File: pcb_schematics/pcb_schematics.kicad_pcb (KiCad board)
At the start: 2 copper layers, 140 x 108 mm, 56 parts, among them J1 CUE_SJ1-352XNG, J2 Conn_01x01_Pin, SW1 SW_Push, SW2 SW_Push, SW3 SW_Push, SW4 SW_Push, SW5 RotaryEncoder, SW6 RotaryEncoder, U1 RPi_Pico_TH, U2 RDA5807M_Module, U3 LM386, U4 LM386

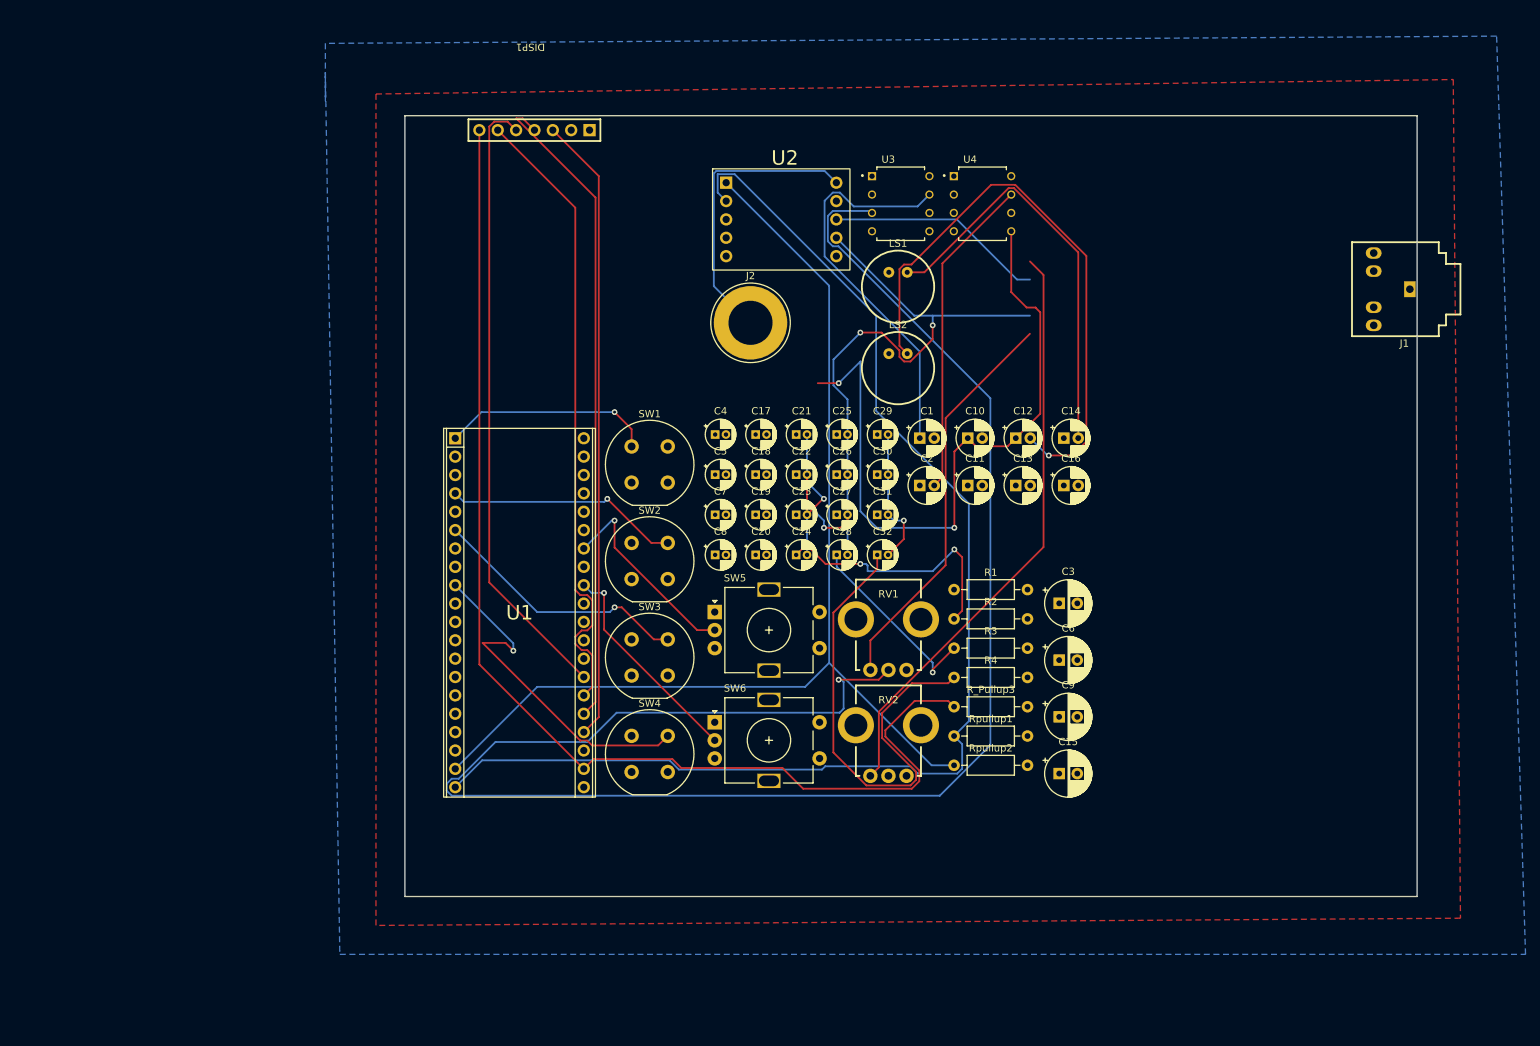
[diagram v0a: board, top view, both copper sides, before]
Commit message: Converted to connectors
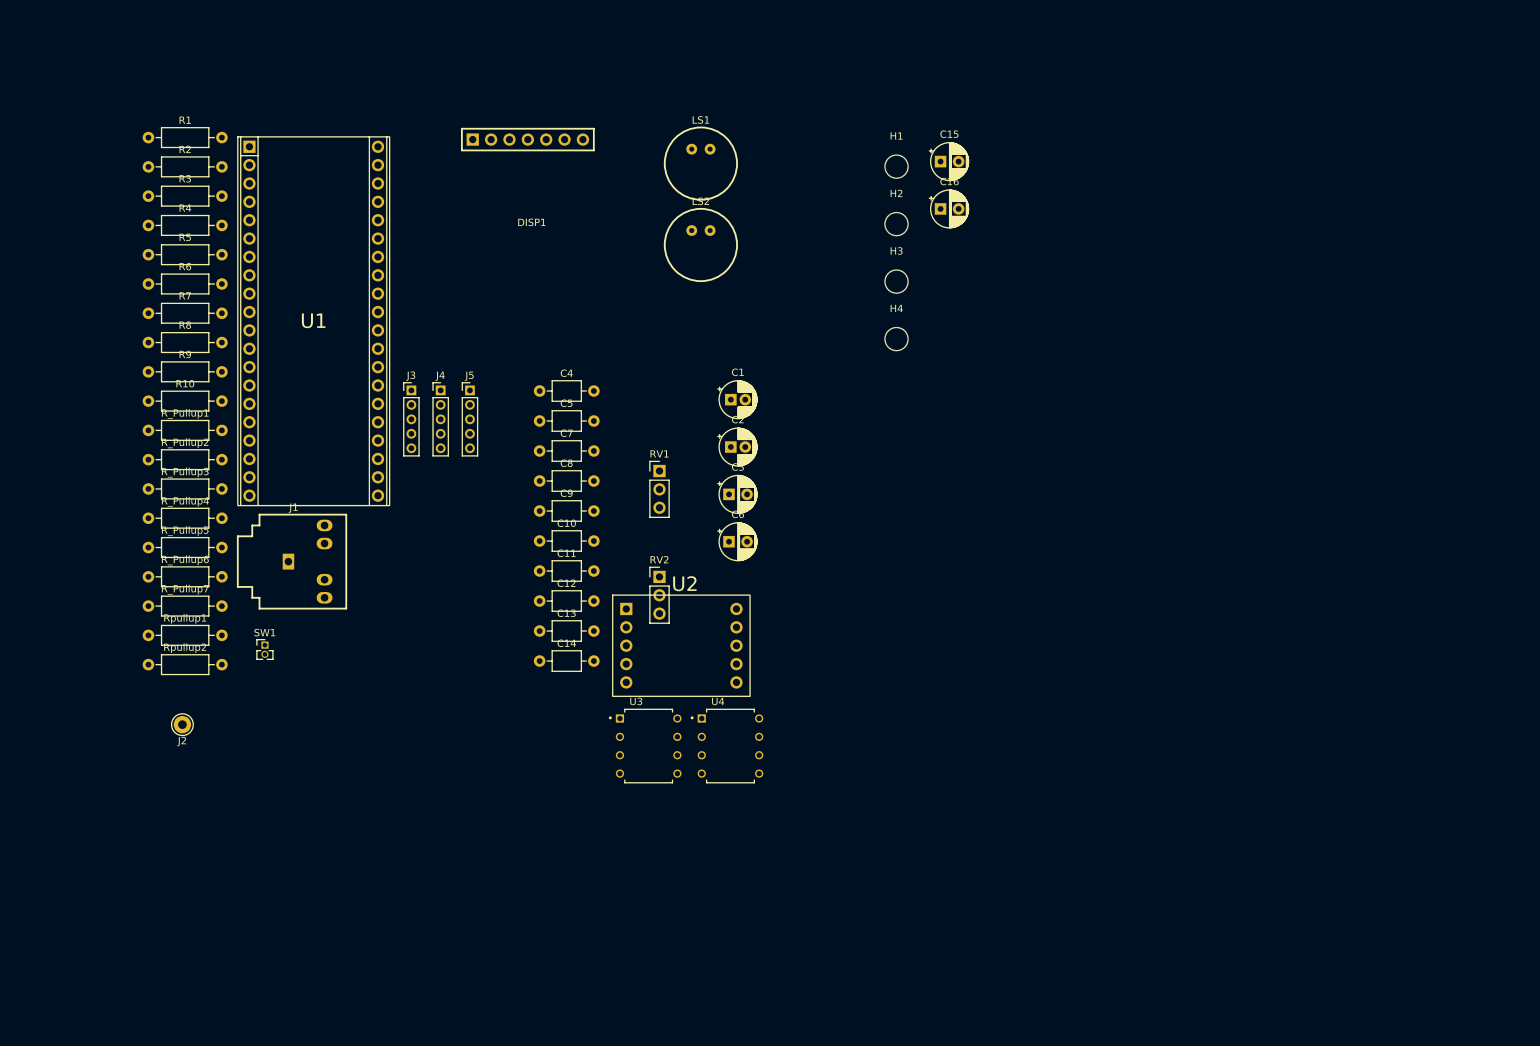
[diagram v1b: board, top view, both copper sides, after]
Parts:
- removed C17, C18, C19, C20, C21, C22, C23, C24, C25, C26, C27, C28, C29, C30, C31, C32: 10 nF, Capacitor_THT:CP_Radial_D4.0mm_P1.50mm
- removed SW2, SW3, SW4: SW_Push, Button_Switch_THT:Push_E-Switch_KS01Q01
- removed SW5, SW6: RotaryEncoder, Rotary_Encoder:RotaryEncoder_Alps_EC11E-Switch_Vertical_H20mm
- added H1: MountingHole, MountingHole:MountingHole_3.2mm_M3, F.Cu at (145.0, 36.0)
- added H2: MountingHole, MountingHole:MountingHole_3.2mm_M3, F.Cu at (145.0, 44.0)
- added H3: MountingHole, MountingHole:MountingHole_3.2mm_M3, F.Cu at (145.0, 52.0)
- added H4: MountingHole, MountingHole:MountingHole_3.2mm_M3, F.Cu at (145.0, 59.9)
- added J3: Conn_01x05, Connector_PinHeader_2.00mm:PinHeader_1x05_P2.00mm_Vertical, F.Cu at (77.9, 67.0)
- added J4: Conn_01x05, Connector_PinHeader_2.00mm:PinHeader_1x05_P2.00mm_Vertical, F.Cu at (82.0, 67.0)
- added J5: Conn_01x05, Connector_PinHeader_2.00mm:PinHeader_1x05_P2.00mm_Vertical, F.Cu at (86.0, 67.0)
- added R10: 10Ω, Resistor_THT:R_Axial_DIN0207_L6.3mm_D2.5mm_P10.16mm_Horizontal, F.Cu at (41.5, 68.5)
- added R5: 10Ω, Resistor_THT:R_Axial_DIN0207_L6.3mm_D2.5mm_P10.16mm_Horizontal, F.Cu at (41.5, 48.2)
- added R6: 10Ω, Resistor_THT:R_Axial_DIN0207_L6.3mm_D2.5mm_P10.16mm_Horizontal, F.Cu at (41.5, 52.3)
- added R7: 10Ω, Resistor_THT:R_Axial_DIN0207_L6.3mm_D2.5mm_P10.16mm_Horizontal, F.Cu at (41.5, 56.3)
- added R8: 10Ω, Resistor_THT:R_Axial_DIN0207_L6.3mm_D2.5mm_P10.16mm_Horizontal, F.Cu at (41.5, 60.4)
- added R9: 10Ω, Resistor_THT:R_Axial_DIN0207_L6.3mm_D2.5mm_P10.16mm_Horizontal, F.Cu at (41.5, 64.4)
- added R_Pullup1: 2kΩ, Resistor_THT:R_Axial_DIN0207_L6.3mm_D2.5mm_P10.16mm_Horizontal, F.Cu at (41.5, 72.5)
- added R_Pullup2: 2kΩ, Resistor_THT:R_Axial_DIN0207_L6.3mm_D2.5mm_P10.16mm_Horizontal, F.Cu at (41.5, 76.6)
- added R_Pullup4: 2kΩ, Resistor_THT:R_Axial_DIN0207_L6.3mm_D2.5mm_P10.16mm_Horizontal, F.Cu at (41.5, 84.7)
- added R_Pullup5: 2kΩ, Resistor_THT:R_Axial_DIN0207_L6.3mm_D2.5mm_P10.16mm_Horizontal, F.Cu at (41.5, 88.7)
- added R_Pullup6: 2kΩ, Resistor_THT:R_Axial_DIN0207_L6.3mm_D2.5mm_P10.16mm_Horizontal, F.Cu at (41.5, 92.8)
- added R_Pullup7: 2kΩ, Resistor_THT:R_Axial_DIN0207_L6.3mm_D2.5mm_P10.16mm_Horizontal, F.Cu at (41.5, 96.8)
- C10, C11, C12, C13, C14: value 10 µF -> 0.05 µF; footprint Capacitor_THT:CP_Radial_D5.0mm_P2.00mm -> Capacitor_THT:C_Axial_L3.8mm_D2.6mm_P7.50mm_Horizontal
- C15, C3, C6: footprint Capacitor_THT:CP_Radial_D6.3mm_P2.50mm -> Capacitor_THT:CP_Radial_D5.0mm_P2.50mm
- C16: value 10 µF -> 470 µF; footprint Capacitor_THT:CP_Radial_D5.0mm_P2.00mm -> Capacitor_THT:CP_Radial_D5.0mm_P2.50mm
- C4, C5, C7, C8: value 10 nF -> 0.05 µF; footprint Capacitor_THT:CP_Radial_D4.0mm_P1.50mm -> Capacitor_THT:C_Axial_L3.8mm_D2.6mm_P7.50mm_Horizontal
- C9: value 470 µF -> 0.05 µF; footprint Capacitor_THT:CP_Radial_D6.3mm_P2.50mm -> Capacitor_THT:C_Axial_L3.8mm_D2.6mm_P7.50mm_Horizontal
- J2: footprint Connector:Banana_Jack_1Pin -> Connector_Pin:Pin_D1.0mm_L10.0mm_LooseFit
- RV1, RV2: footprint ECE:Bourns_PTV09_Horiz -> Connector_PinHeader_2.54mm:PinHeader_1x03_P2.54mm_Vertical
- SW1: footprint Button_Switch_THT:Push_E-Switch_KS01Q01 -> Connector_PinHeader_1.27mm:PinHeader_1x02_P1.27mm_Vertical
- moved J1 159.6 mm to (60.9, 90.7), turned to 0 degrees
- moved R1 127.8 mm to (41.5, 32.0)
- moved R2 127.8 mm to (41.5, 36.1)
- moved R3 127.8 mm to (41.5, 40.1)
- moved R4 127.8 mm to (41.5, 44.2)
- moved R_Pullup3 115.4 mm to (41.5, 80.6)
- moved Rpullup1 112.3 mm to (41.5, 100.9)
- moved Rpullup2 112.3 mm to (41.5, 104.9)
- moved J2 96.2 mm to (46.2, 113.2)
- moved C15 86.2 mm to (151.1, 35.4)
- moved U3 82.7 mm to (110.7, 116.2)
- moved U4 82.7 mm to (122.0, 116.2)
- moved C14 78.8 mm to (95.6, 104.4)
- moved C9 77.3 mm to (95.6, 83.7)
- moved DISP1 74.7 mm to (76.3, 64.3), turned to 0 degrees
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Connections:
- C10 pad 1: Net-(C10-Pad1) -> /ROT1A
- C11 pad 1: Net-(C10-Pad2) -> /ROT2A
- C12 pad 1: Net-(C10-Pad1) -> /ROT2B
- C12 pad 2: Net-(C11-Pad2) -> Net-(C12-Pad2)
- C13 pad 1: Net-(C13-Pad1) -> /ROT3A
- C14 pad 1: Net-(C13-Pad1) -> /ROT3B
- C15 pad 2: Net-(C14-Pad2) -> Net-(U3-+)
- C16 pad 1: Net-(C13-Pad2) -> Net-(C16-Pad1)
- C16 pad 2: Net-(C14-Pad2) -> Net-(U4-+)
- C2 pad 1: GND -> Net-(U4-BYPASS)
- C2 pad 2: Net-(U4-BYPASS) -> GND
- C3 pad 1: Net-(C10-Pad1) -> Net-(C3-Pad1)
- C4 pad 1: Net-(C17-Pad1) -> Net-(C3-Pad1)
- C4 pad 2: Net-(C10-Pad1) -> Net-(C4-Pad2)
- C5 pad 1: Net-(C21-Pad1) -> Net-(C5-Pad1)
- C5 pad 2: Net-(C13-Pad1) -> Net-(C5-Pad2)
- C6 pad 1: Net-(C13-Pad1) -> Net-(C5-Pad1)
- C6 pad 2: Net-(C15-Pad1) -> Net-(C6-Pad2)
- C7 pad 1: Net-(C25-Pad1) -> /LOUT
- C7 pad 2: /ROUT -> Net-(C7-Pad2)
- C8 pad 1: Net-(C29-Pad1) -> /ROUT
- C8 pad 2: /LOUT -> Net-(C8-Pad2)
- C9 pad 1: Net-(C3-Pad2) -> /ROT1B
- C9 pad 2: Net-(C11-Pad2) -> Net-(C9-Pad2)
- LS1 pad 1: Net-(C14-Pad2) -> Net-(C6-Pad2)
- LS2 pad 1: Net-(C11-Pad2) -> Net-(C3-Pad2)
- R1 pad 1: Net-(C17-Pad1) -> Net-(C4-Pad2)
- R2 pad 1: Net-(C21-Pad1) -> Net-(C5-Pad2)
- R3 pad 1: Net-(C25-Pad1) -> Net-(C8-Pad2)
- R4 pad 1: Net-(C29-Pad1) -> Net-(C7-Pad2)
- RV1 pad 2: Net-(U3-+) -> Net-(C15-Pad1)
- RV2 pad 2: Net-(U4-+) -> Net-(C16-Pad1)
- U1 pad 10: unconnected-(U1-GP7-Pad10) -> /ROT2B
- U1 pad 2: unconnected-(U1-GP1-Pad2) -> /SW2
- U1 pad 32: /RotB -> /ROT3B
- U1 pad 34: /RotA -> /ROT3A
- U1 pad 39: unconnected-(U1-VSYS-Pad39) -> 5V
- U1 pad 4: /SW2 -> /SW3
- U1 pad 5: unconnected-(U1-GP3-Pad5) -> /SW4
- U1 pad 6: /SW3 -> /ROT1A
- U1 pad 7: unconnected-(U1-GP5-Pad7) -> /ROT1B
- U1 pad 9: /SW4 -> /ROT2A
- U3 pad 5: Net-(C13-Pad1) -> Net-(C5-Pad1)
- U3 pad 6: /3V3 -> 5V
- U4 pad 5: Net-(C10-Pad1) -> Net-(C3-Pad1)
- U4 pad 6: /3V3 -> 5V
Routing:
- net Net-(U3-+): track 240.0 -> 0.00 mm, vias 1 -> 0
- net /I2CSCK: track 176.6 -> 0.00 mm
- net /CS: track 163.9 -> 0.00 mm
- net /I2CTX: track 153.2 -> 0.00 mm
- net Net-(C10-Pad1): track 94.9 -> 0.00 mm, vias 2 -> 0
- net /SDA: track 90.7 -> 0.00 mm
- net /ROUT: track 89.0 -> 0.00 mm, vias 3 -> 0
- net /DC: track 87.5 -> 0.00 mm
- net /SCK: track 86.8 -> 0.00 mm
- net /RES: track 86.0 -> 0.00 mm
- net Net-(C11-Pad2): track 82.1 -> 0.00 mm, vias 1 -> 0
- net /RSpeaker: track 81.8 -> 0.00 mm
- net Net-(C29-Pad1): track 66.7 -> 0.00 mm
- net Net-(C14-Pad2): track 57.9 -> 0.00 mm
- net /LSpeaker: track 55.7 -> 0.00 mm
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- removed copper zone on B.Cu, net /3V3
- removed copper zone on F.Cu, net GND
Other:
- board outline removed

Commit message: Updates PCb according to ROB's feedback
Added PCb layour according to the discussion with butoons and display on top and display below using front copper. Added Radio module using back copper. Speakers left to set up using back copper.
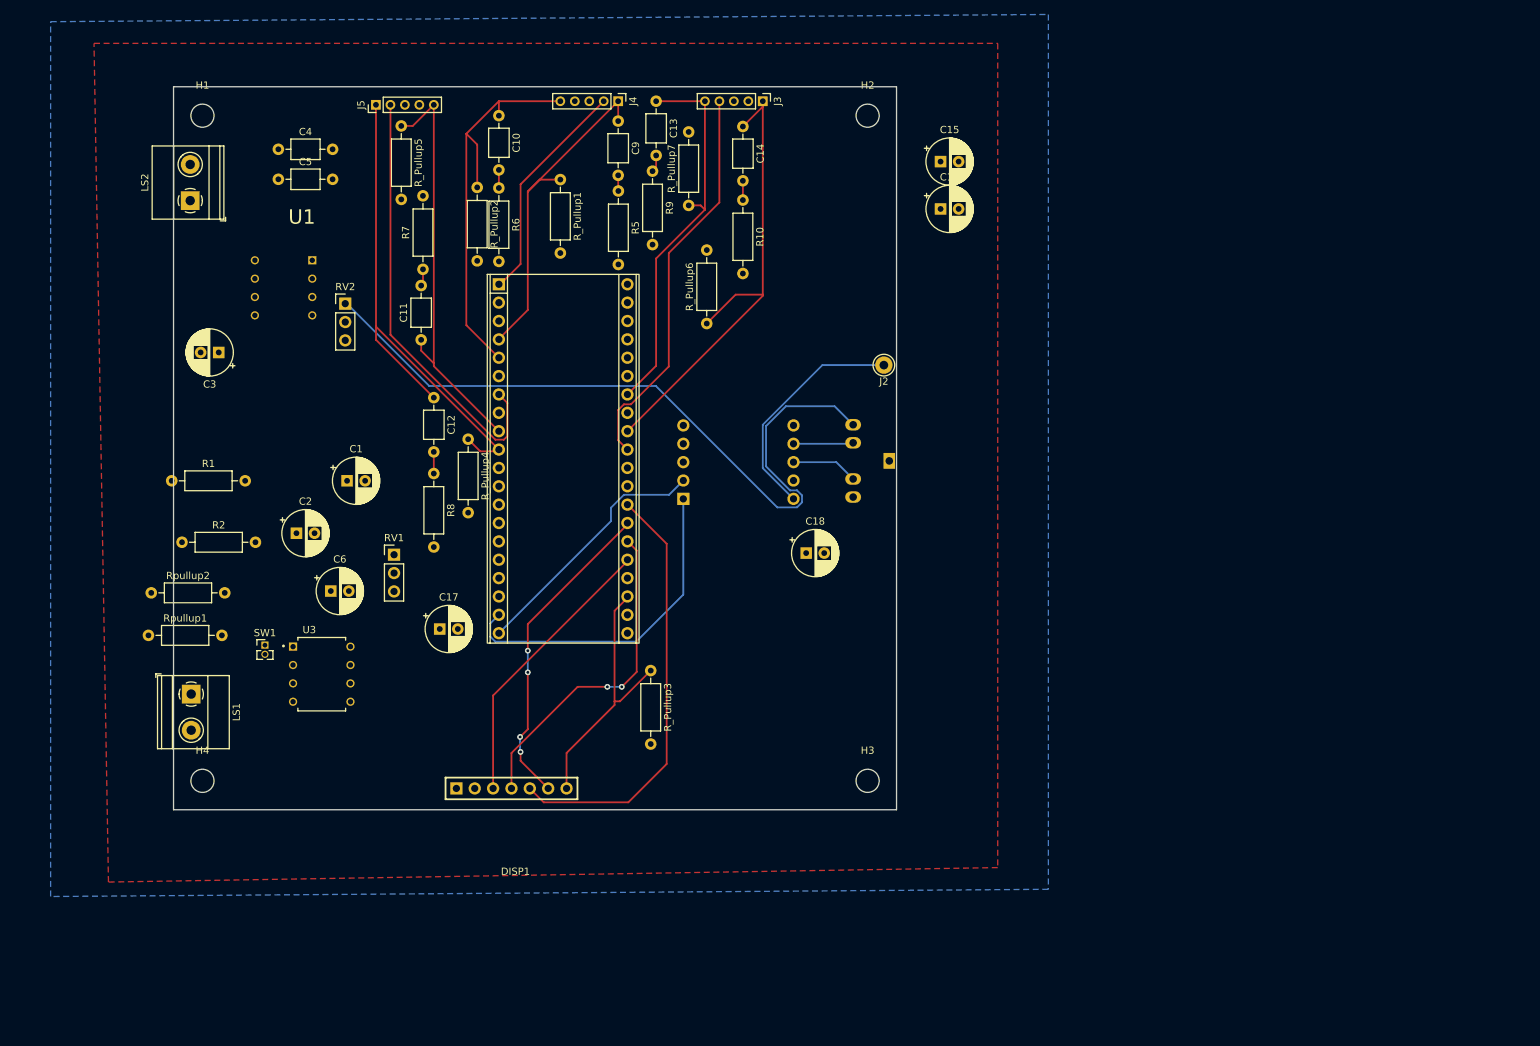
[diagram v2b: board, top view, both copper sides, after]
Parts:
- removed C7, C8: 0.05 µF, Capacitor_THT:C_Axial_L3.8mm_D2.6mm_P7.50mm_Horizontal
- removed R3, R4: 10Ω, Resistor_THT:R_Axial_DIN0207_L6.3mm_D2.5mm_P10.16mm_Horizontal
- added C17: 10 µF, Capacitor_THT:CP_Radial_D6.3mm_P2.50mm, F.Cu at (81.8, 100.0)
- added C18: 10 µF, Capacitor_THT:CP_Radial_D6.3mm_P2.50mm, F.Cu at (132.5, 89.5)
- C1, C2: footprint Capacitor_THT:CP_Radial_D5.0mm_P2.00mm -> Capacitor_THT:CP_Radial_D6.3mm_P2.50mm
- C15, C16, C3, C6: footprint Capacitor_THT:CP_Radial_D5.0mm_P2.50mm -> Capacitor_THT:CP_Radial_D6.3mm_P2.50mm
- J1, U2, U4: moved to B.Cu
- LS1, LS2: footprint ECE:CUE_CMA-4544PF-W -> TerminalBlock_Phoenix:TerminalBlock_Phoenix_MKDS-1,5-2_1x02_P5.00mm_Horizontal
- moved H4 113.8 mm to (49.0, 121.0)
- moved J2 109.0 mm to (143.2, 63.5)
- moved LS1 101.7 mm to (47.4, 109.0), turned to -90 degrees
- moved H1 96.3 mm to (49.0, 29.0)
- moved R_Pullup7 93.0 mm to (116.2, 41.4), turned to 90 degrees
- moved DISP1 89.8 mm to (74.0, 154.0)
- moved U4 88.5 mm to (60.2, 52.8), turned to 180 degrees
- moved R10 86.8 mm to (123.8, 40.7), turned to -90 degrees
- moved R_Pullup6 84.8 mm to (118.8, 57.8), turned to 90 degrees
- moved J1 84.3 mm to (144.0, 76.8), turned to 180 degrees
- moved C14 79.1 mm to (123.8, 30.5), turned to -90 degrees
- moved R9 75.0 mm to (111.2, 36.7), turned to -90 degrees
- moved C13 75.0 mm to (111.8, 27.0), turned to -90 degrees
- moved R_Pullup3 73.9 mm to (111.0, 105.8), turned to -90 degrees
- moved C3 73.3 mm to (51.2, 61.8), turned to 180 degrees
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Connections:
- J1 pad 4: /LOUT -> /ROUT
- J1 pad 5: /ROUT -> /LOUT
- U1 pad 31: unconnected-(U1-GP26/ADC0-Pad31) -> /SW3
- U1 pad 4: /SW3 -> /ROT1B
- U1 pad 5: /SW4 -> /ROT1A
- U1 pad 6: /ROT1A -> unconnected-(U1-GP4-Pad6)
- U1 pad 7: /ROT1B -> /SW4
- U3 pad 1: unconnected-(U3-GAIN-Pad1) -> Net-(C17-Pad1)
- U3 pad 8: unconnected-(U3-GAIN-Pad8) -> Net-(C17-Pad2)
- U4 pad 1: unconnected-(U4-GAIN-Pad1) -> Net-(C18-Pad1)
- U4 pad 8: unconnected-(U4-GAIN-Pad8) -> Net-(C18-Pad2)
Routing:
- net /RSpeaker: track 0.00 -> 102.6 mm
- net /ROT2B: track 0.00 -> 72.9 mm
- net /ROT3B: track 0.00 -> 67.4 mm
- net /SW4: track 0.00 -> 60.4 mm
- net /RES: track 0.00 -> 59.9 mm
- net /ROT2A: track 0.00 -> 58.6 mm
- net /ROT1A: track 0.00 -> 57.7 mm
- net /SW3: track 0.00 -> 55.1 mm
- net /ROT3A: track 0.00 -> 54.2 mm
- net /ROT1B: track 0.00 -> 47.5 mm
- net /I2CTX: track 0.00 -> 46.4 mm
- net /SDA: track 0.00 -> 45.3 mm, vias 0 -> 2
- net /DC: track 0.00 -> 44.4 mm, vias 0 -> 4
- net /SCK: track 0.00 -> 39.3 mm
- net /CS: track 0.00 -> 36.8 mm
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- added copper zone on F.Cu, net /3V3
- added copper zone on B.Cu, net GND
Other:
- board outline added: 100 x 100 mm
